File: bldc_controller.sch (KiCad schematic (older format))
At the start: 147 parts, among them J1 Conn_01x06_Male, J2 Banana_Jack, J3 Banana_Jack, Q1 2N7002E, Q10 IRLB8721PBF, Q11 IRLB8721PBF, Q2 DMN65D8L-7, Q3 DMN65D8L-7, Q4 MMBT3904, Q5 IRF4905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

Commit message: Manual Revert
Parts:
- D10, D11: footprint Diode_THT:D_DO-35_SOD27_P7.62mm_Horizontal -> Diode_SMD:D_SOD-323_HandSoldering
- D14, D15, D16: footprint Diode_THT:D_DO-41_SOD81_P10.16mm_Horizontal -> Diode_SMD:D_SOD-123
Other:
- moved on the sheet: C26, C27, C31, C32, R16, R22, R23, RV1, TP12, TP2, TP4, U6A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

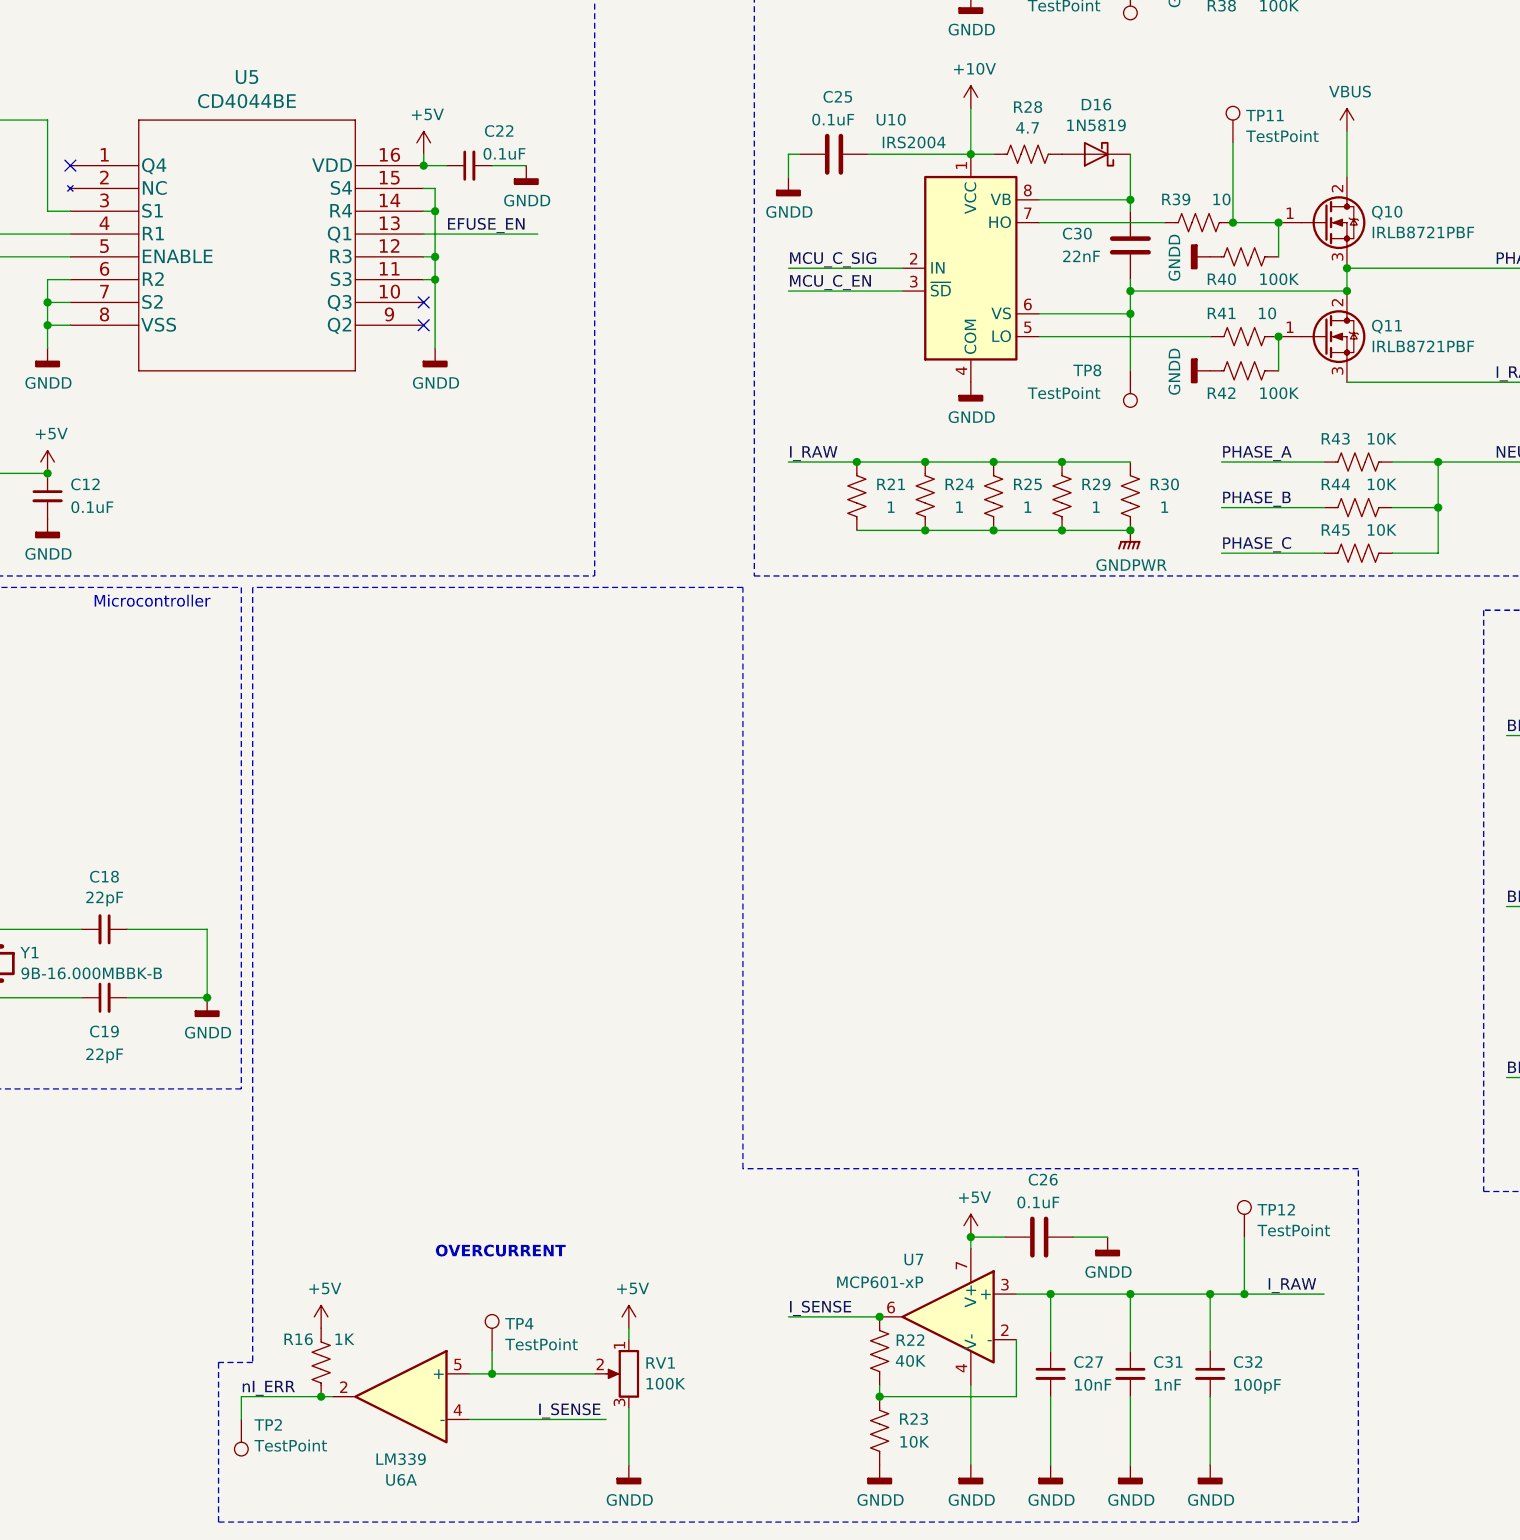
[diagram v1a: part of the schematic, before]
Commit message: added vias for motor
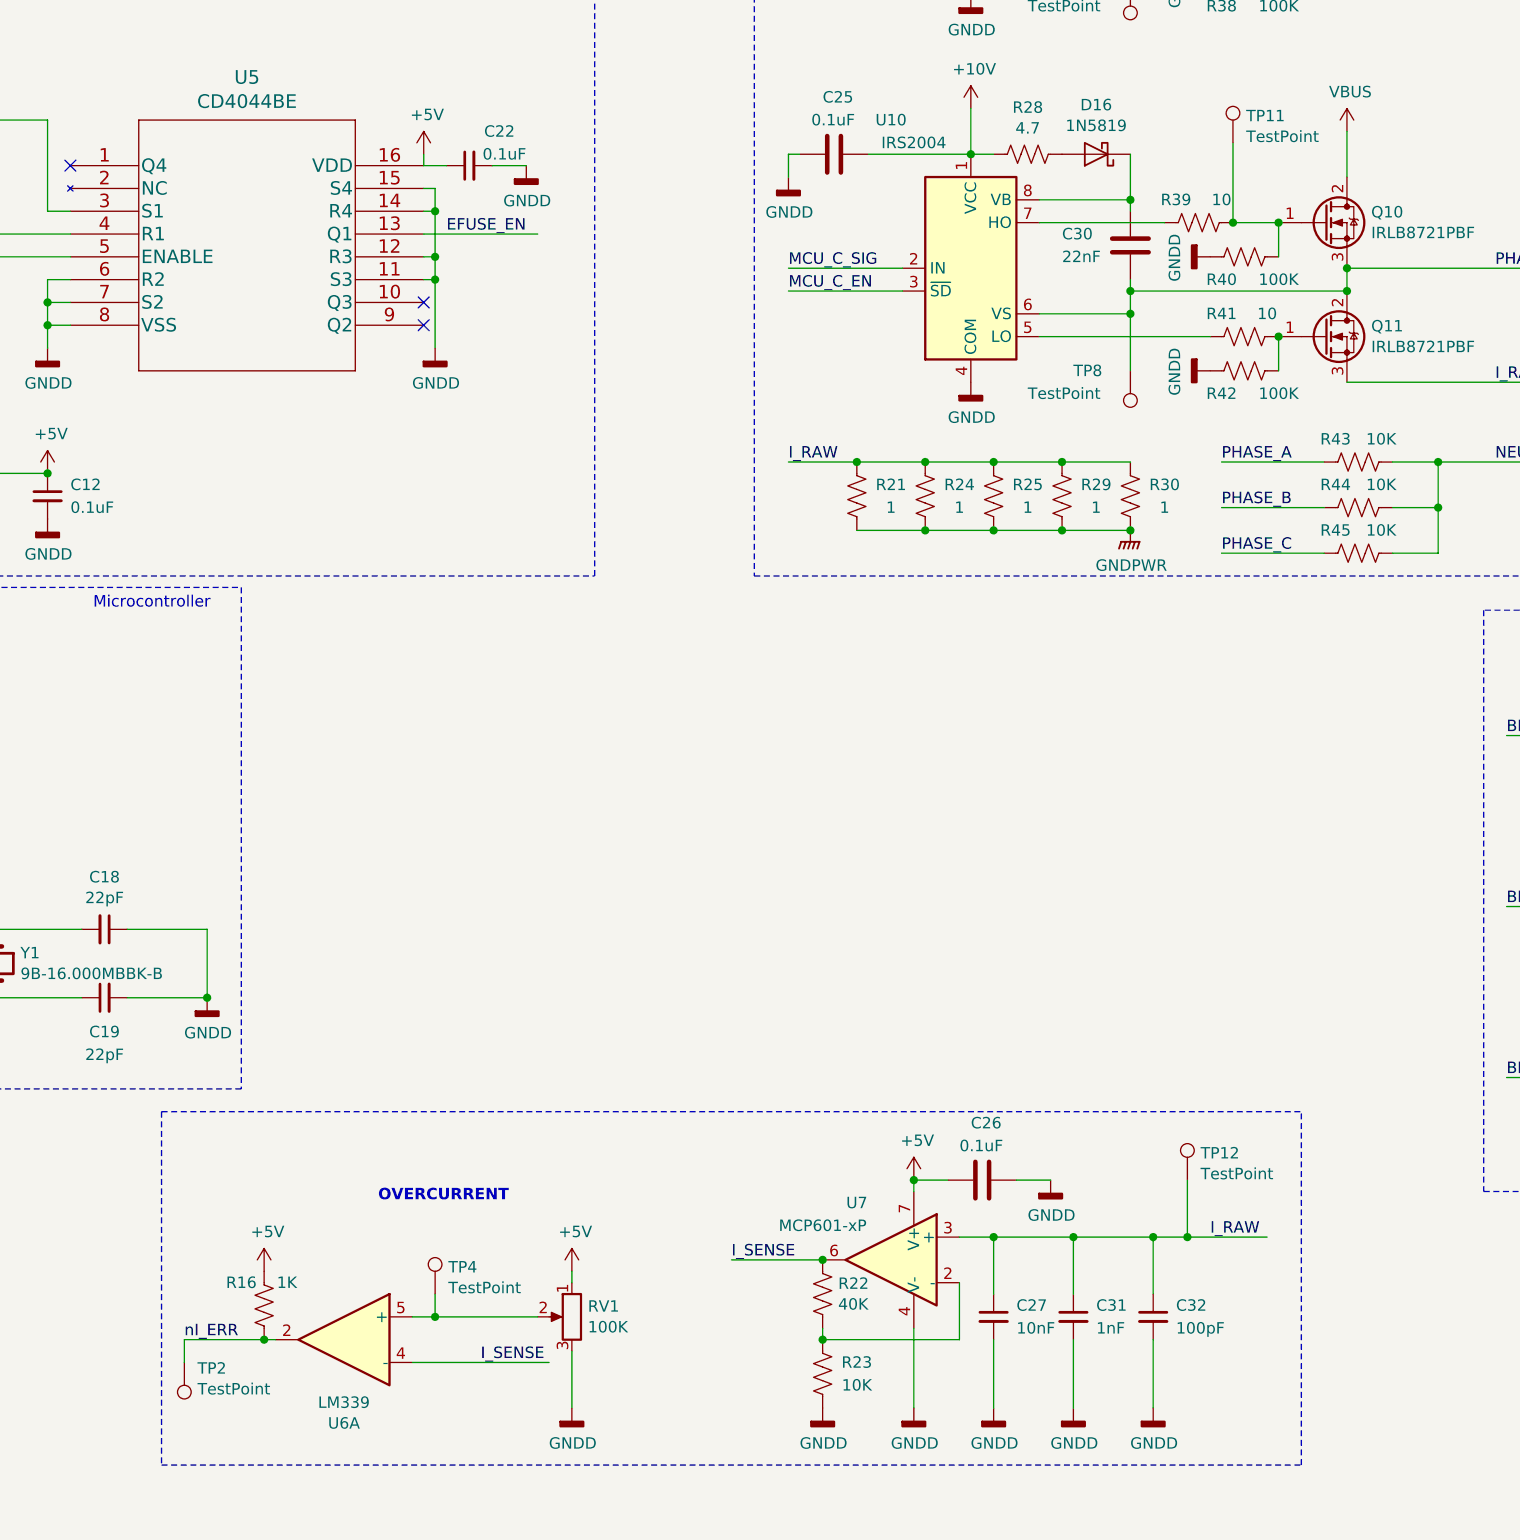
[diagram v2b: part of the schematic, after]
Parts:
- D10, D11: footprint Diode_SMD:D_SOD-323_HandSoldering -> Diode_THT:D_DO-35_SOD27_P7.62mm_Horizontal
- D14, D15, D16: footprint Diode_SMD:D_SOD-123 -> Diode_THT:D_DO-41_SOD81_P10.16mm_Horizontal
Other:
- moved on the sheet: C26, C27, C31, C32, R16, R22, R23, RV1, TP12, TP2, TP4, U6A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
